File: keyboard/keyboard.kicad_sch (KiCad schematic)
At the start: 5 parts

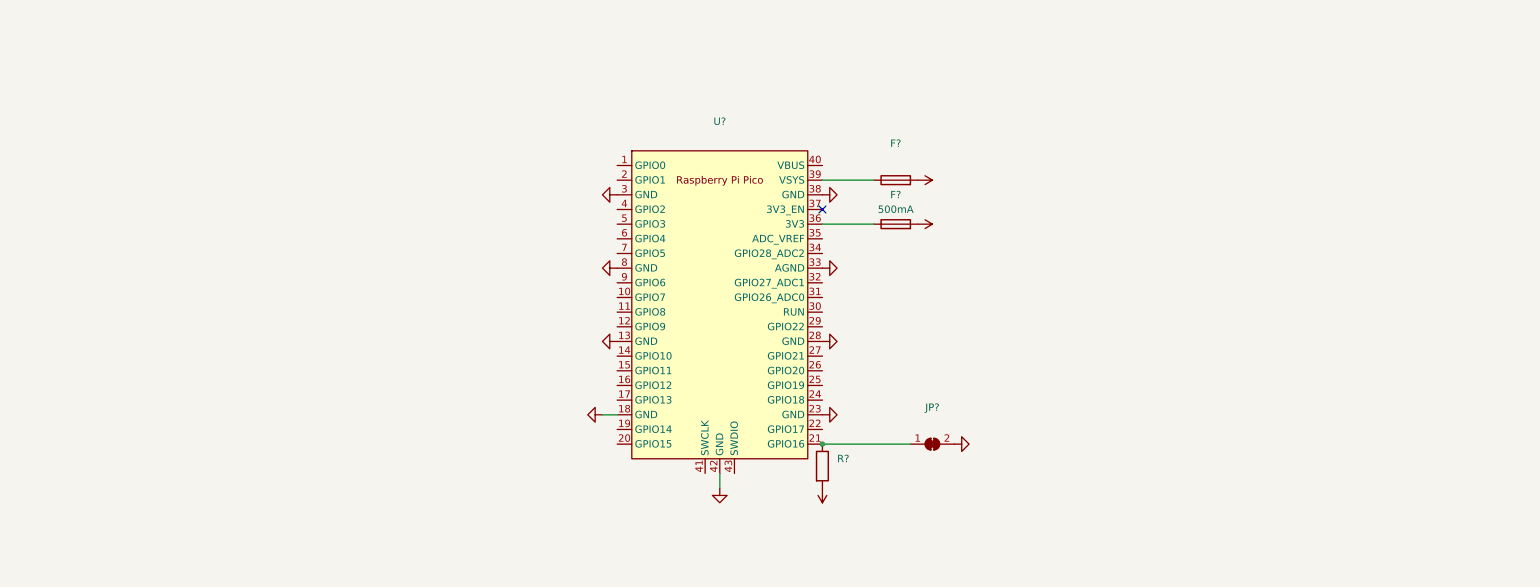
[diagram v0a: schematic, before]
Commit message: Add keyboard PCB layout
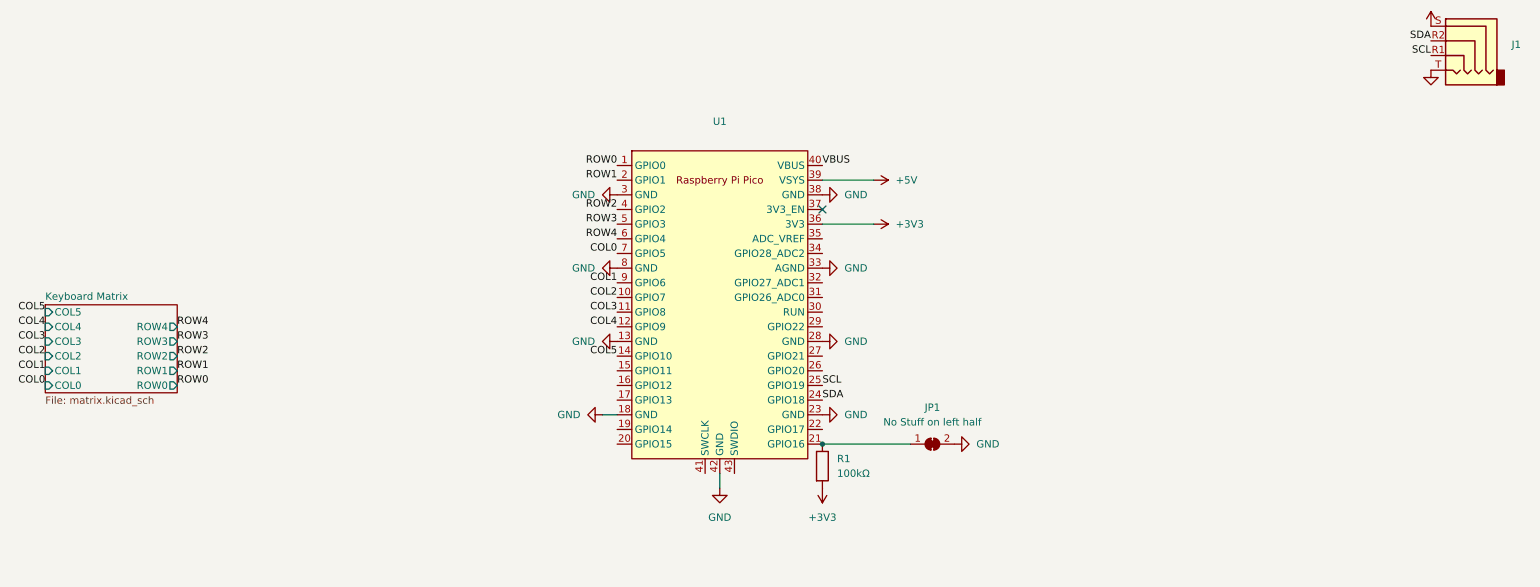
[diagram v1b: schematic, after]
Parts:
- removed F?: 500mA, symbol Device:Fuse
- removed F?: (no value), symbol Device:Fuse
- added J1: (no value), symbol Connector:AudioJack4
- JP1: renamed from JP?; value (none) -> No Stuff on left half; footprint (none) -> Jumper:SolderJumper-2_P1.3mm_Bridged2Bar_Pad1.0x1.5mm
- R1: renamed from R?; value (none) -> 100kΩ; footprint (none) -> Resistor_THT:R_Axial_DIN0207_L6.3mm_D2.5mm_P7.62mm_Horizontal
- gave numbers to parts that had none: 1
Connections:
- net +3V3: now also U1.36 (3V3)
- net +5V: now also U1.39 (VSYS), J1.S
- net GND: now also J1.T
- net ROW0: now reaches U1.1 (GPIO0)
- net COL2: now reaches U1.10 (GPIO7)
- net COL3: now reaches U1.11 (GPIO8)
- net COL4: now reaches U1.12 (GPIO9)
- net COL5: now reaches U1.14 (GPIO10)
- net ROW1: now reaches U1.2 (GPIO1)
- net SDA: now reaches U1.24 (GPIO18)
- net SDA: now also J1.R2
- net SCL: now reaches U1.25 (GPIO19)
- net SCL: now also J1.R1
- net ROW2: now reaches U1.4 (GPIO2)
- net VBUS: now reaches U1.40 (VBUS)
- net ROW3: now reaches U1.5 (GPIO3)
- net ROW4: now reaches U1.6 (GPIO4)
- net COL0: now reaches U1.7 (GPIO5)
- net COL1: now reaches U1.9 (GPIO6)
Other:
- added sheet Keyboard Matrix (matrix.kicad_sch)

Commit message: Redo design
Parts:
- removed J1: (no value), symbol Connector:AudioJack4
- removed JP1: No Stuff on left half, Jumper:SolderJumper-2_P1.3mm_Bridged2Bar_Pad1.0x1.5mm, symbol Jumper:SolderJumper_2_Bridged
- removed R1: 100kΩ, Resistor_THT:R_Axial_DIN0207_L6.3mm_D2.5mm_P7.62mm_Horizontal, symbol Device:R
- removed U1: (no value), symbol rpi-pico:Pico
- added Brd: SSD1306, symbol ssd1306:SSD1306
- added J: Micro_SD_Card, symbol Connector:Micro_SD_Card
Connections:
- net +3V3: now also Brd.2 (VCC), J.4 (VDD)
- net GND: now also Brd.1 (GND), J.6 (VSS), J.9 (SHIELD)
- new net keyboard_common/SCL: Brd.3 (SCL)
- new net keyboard_common/SD0: J.7 (DAT0)
- new net keyboard_common/SD1: J.8 (DAT1)
- new net keyboard_common/SD2: J.1 (DAT2)
- new net keyboard_common/SD3: J.2 (DAT3/CD)
- new net keyboard_common/SDA: Brd.4 (SDA)
- new net keyboard_common/SDCLK: J.5 (CLK)
- new net keyboard_common/SDCMD: J.3 (CMD)
- no-connect marks 1 -> 0
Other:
- removed sheet Keyboard Matrix
- added sheet keyboard_common (keyboard_common.kicad_sch)
- title: (none) -> rkb1
